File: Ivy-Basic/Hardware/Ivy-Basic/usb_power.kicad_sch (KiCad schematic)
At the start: 6 parts, among them J1 USB_C_Receptacle_USB2.0_16P

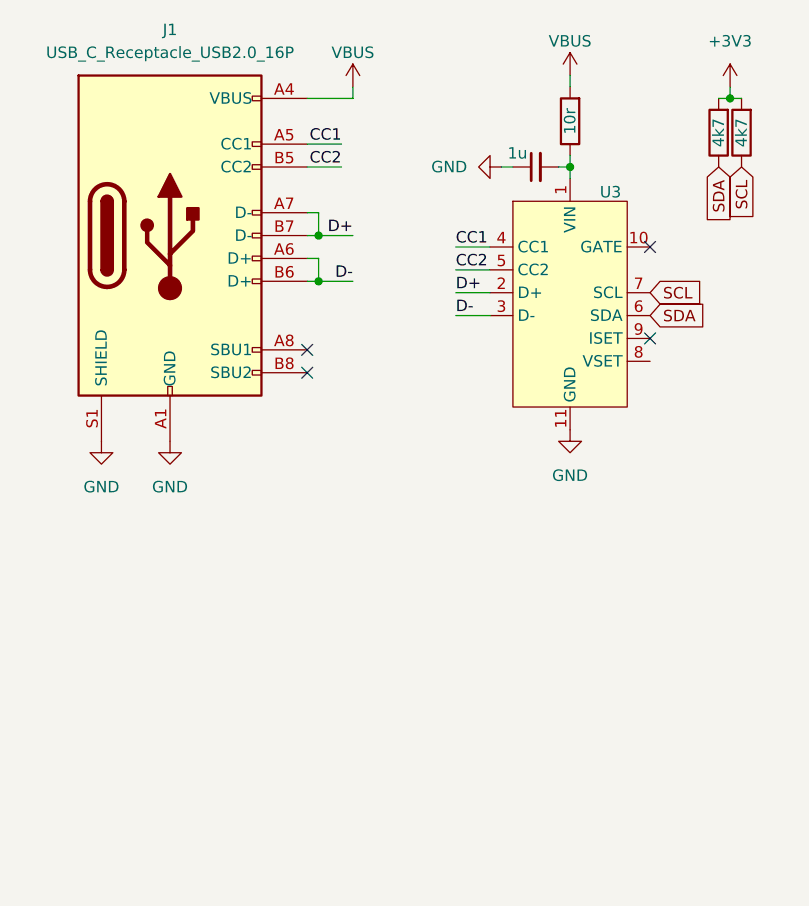
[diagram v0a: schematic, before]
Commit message: add switching buck converter
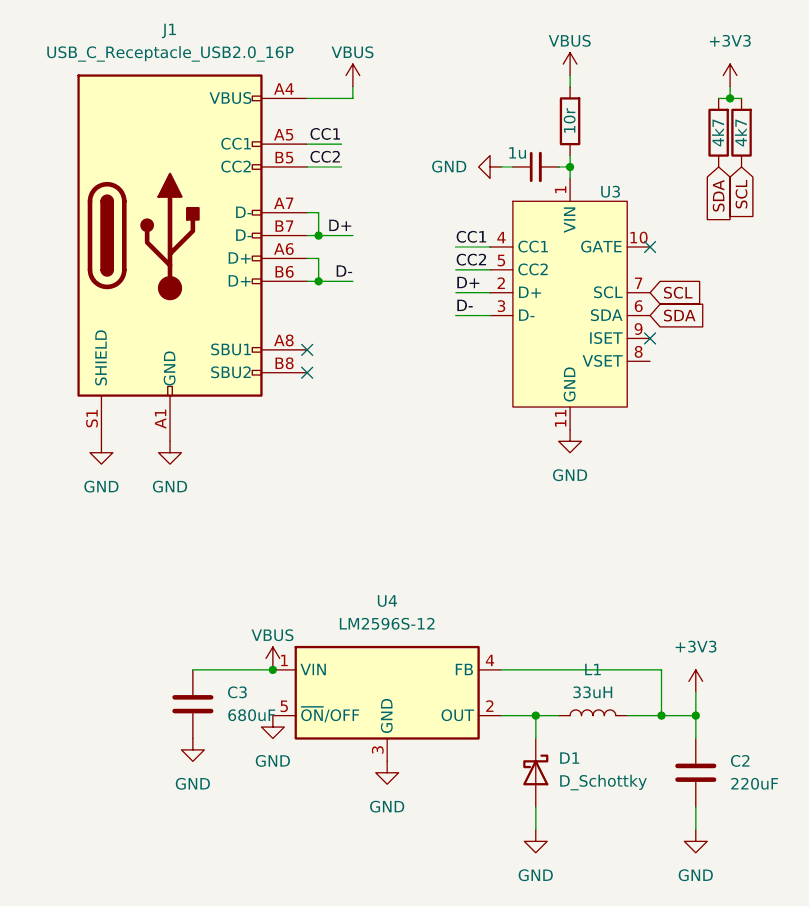
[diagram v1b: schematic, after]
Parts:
- added C2: 220uF, symbol Device:C
- added C3: 680uF, symbol Device:C
- added D1: D_Schottky, symbol Device:D_Schottky
- added L1: 33uH, symbol Device:L
- added U4: LM2596S-12, Package_TO_SOT_SMD:TO-263-5_TabPin3, symbol Regulator_Switching:LM2596S-12
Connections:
- net +3V3: now also C2.1, L1.2, U4.4 (FB)
- net GND: now also C2.2, C3.2, D1.2 (A), U4.3 (GND), U4.5 (~{ON}/OFF)
- net VBUS: now also C3.1, U4.1 (VIN)
- new net: D1.1 (K), L1.1, U4.2 (OUT)
